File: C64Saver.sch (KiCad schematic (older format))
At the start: 15 parts, among them J1 Power I/O, Q1 PN2222A, Q2 PN2222A

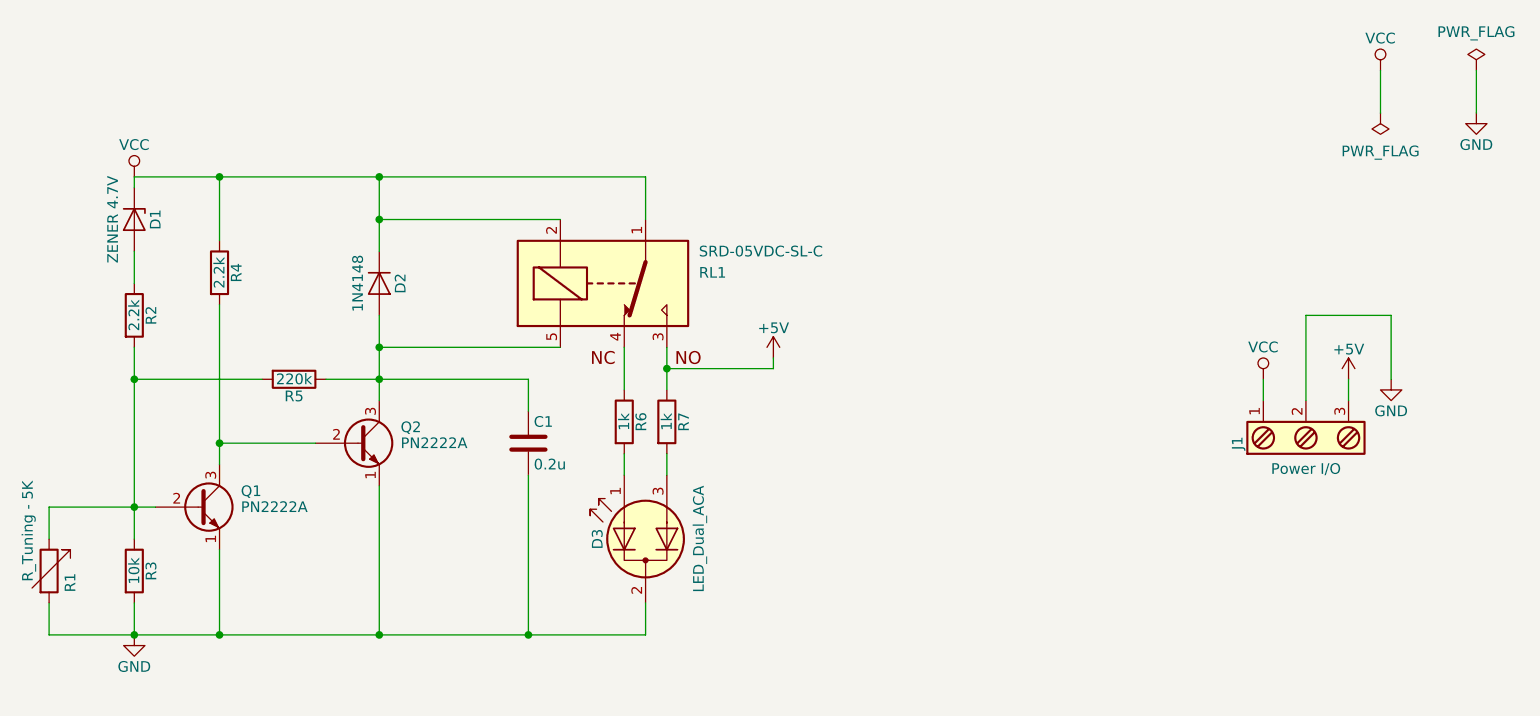
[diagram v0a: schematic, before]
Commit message: Relabel some components
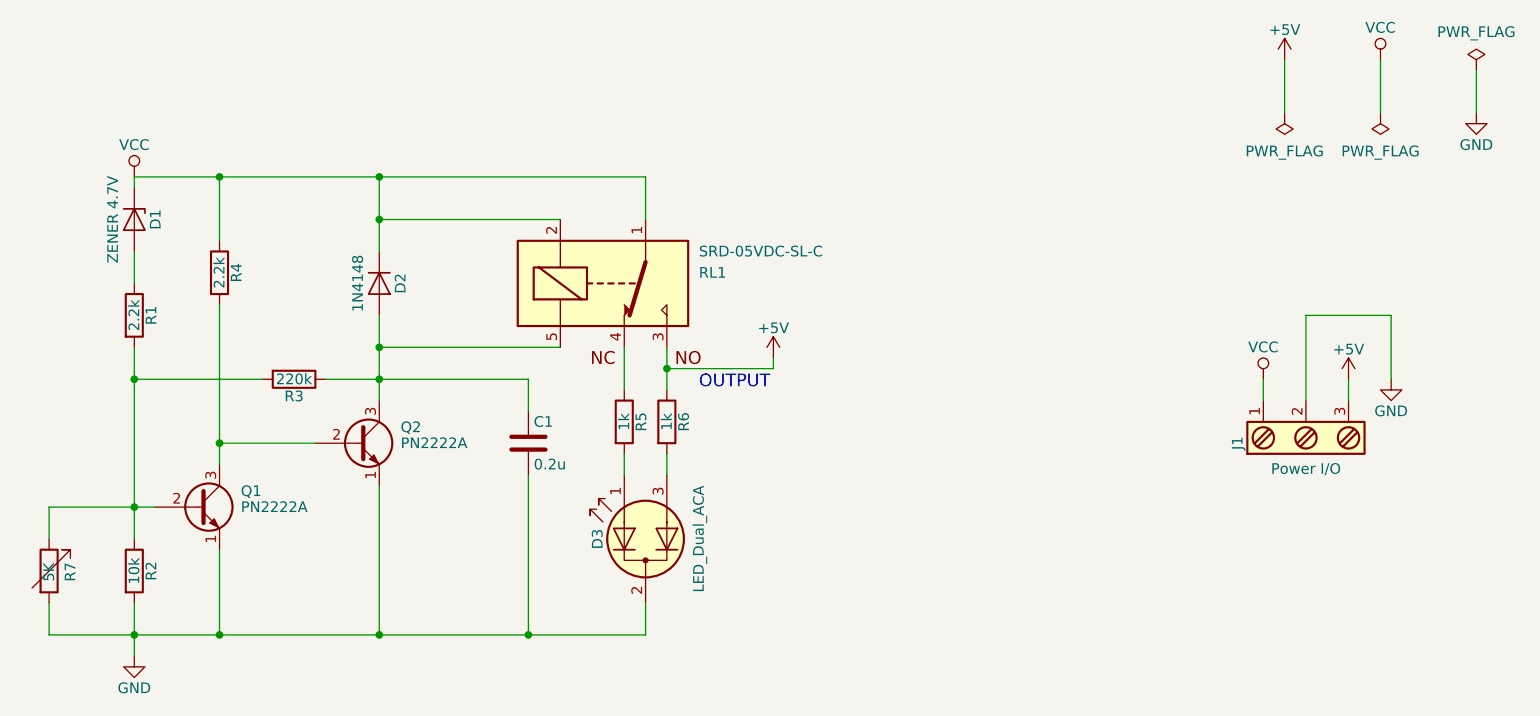
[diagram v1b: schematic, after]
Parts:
- R7: renamed from R1; value R_Tuning - 5K -> 5K
- renumbered R2 to R1, R3 to R2, R5 to R3, R6 to R5, R7 to R6
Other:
- note added: "OUTPUT"
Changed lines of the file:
@@
 $EndComp
 $Comp
-L R R3
+L R R2
 U 1 1 59765DBB
 P 4200 3200
-F 0 "R3" V 4280 3200 50  0000 C CNN
+F 0 "R2" V 4280 3200 50  0000 C CNN
 F 1 "10k" V 4200 3200 50  0000 C CNN
 F 2 "Resistors_SMD:R_0805_HandSoldering" V 4130 3200 50  0001 C CNN
@@
 L GND #PWR01
 U 1 1 59765E30
-P 4200 3500
-F 0 "#PWR01" H 4200 3250 50  0001 C CNN
-F 1 "GND" H 4200 3350 50  0000 C CNN
-F 2 "" H 4200 3500 50  0000 C CNN
-F 3 "" H 4200 3500 50  0000 C CNN
-	1    4200 3500
-	1    0    0    -1
-$EndComp
-$Comp
-L R R2
+P 4200 3600
+F 0 "#PWR01" H 4200 3350 50  0001 C CNN
+F 1 "GND" H 4200 3450 50  0000 C CNN
+F 2 "" H 4200 3600 50  0000 C CNN
+F 3 "" H 4200 3600 50  0000 C CNN
+	1    4200 3600
+	1    0    0    -1
+$EndComp
+$Comp
+L R R1
 U 1 1 59765E4A
 P 4200 2000
-F 0 "R2" V 4280 2000 50  0000 C CNN
+F 0 "R1" V 4280 2000 50  0000 C CNN
 F 1 "2.2k" V 4200 2000 50  0000 C CNN
 F 2 "Resistors_SMD:R_0805_HandSoldering" V 4130 2000 50  0001 C CNN
@@
 $EndComp
 $Comp
-L R R5
+L R R3
 U 1 1 5976603D
 P 4950 2300
-F 0 "R5" V 5030 2300 50  0000 C CNN
+F 0 "R3" V 5030 2300 50  0000 C CNN
 F 1 "220k" V 4950 2300 50  0000 C CNN
 F 2 "Resistors_SMD:R_0805_HandSoldering" V 4880 2300 50  0001 C CNN
@@
 	3800 2900 4300 2900
 Wire Wire Line
-	4200 3350 4200 3500
+	4200 3350 4200 3600
 Wire Wire Line
 	3800 3500 6600 3500
@@
 Connection ~ 5350 2150
 $Comp
-L R R6
+L R R5
 U 1 1 597671B5
 P 6500 2500
-F 0 "R6" V 6580 2500 50  0000 C CNN
+F 0 "R5" V 6580 2500 50  0000 C CNN
 F 1 "1k" V 6500 2500 50  0000 C CNN
 F 2 "Resistors_SMD:R_0805_HandSoldering" V 6430 2500 50  0001 C CNN
@@
 L VCC #PWR08
 U 1 1 59767AEF
-P 10050 850
-F 0 "#PWR08" H 10050 700 50  0001 C CNN
-F 1 "VCC" H 10050 1000 50  0000 C CNN
-F 2 "" H 10050 850 50  0000 C CNN
-F 3 "" H 10050 850 50  0000 C CNN
-	1    10050 850
+P 10050 800
+F 0 "#PWR08" H 10050 650 50  0001 C CNN
+F 1 "VCC" H 10050 950 50  0000 C CNN
+F 2 "" H 10050 800 50  0000 C CNN
+F 3 "" H 10050 800 50  0000 C CNN
+	1    10050 800
 	1    0    0    -1
 $EndComp
@@
 $EndComp
 Wire Wire Line
-	10050 850  10050 1050
+	10050 800  10050 1050
 Wire Wire Line
 	10500 850  10500 1050
@@
 	6600 3500 6600 3350
 $Comp
-L R R7
+L R R6
 U 1 1 59768A52
 P 6700 2500
-F 0 "R7" V 6780 2500 50  0000 C CNN
+F 0 "R6" V 6780 2500 50  0000 C CNN
 F 1 "1k" V 6700 2500 50  0000 C CNN
 F 2 "Resistors_SMD:R_0805_HandSoldering" V 6630 2500 50  0001 C CNN
@@
 Connection ~ 6700 2250
 $Comp
-L R_Variable R1
+L R_Variable R7
 U 1 1 59768CBA
 P 3800 3200
-F 0 "R1" V 3900 3100 50  0000 L CNN
-F 1 "R_Tuning - 5K" V 3700 3150 50  0000 L CNN
+F 0 "R7" V 3900 3150 50  0000 L CNN
+F 1 "5K" V 3800 3150 50  0000 L CNN
 F 2 "pth_resistors:trimmer_vishay_64w" V 3730 3200 50  0001 C CNN
 F 3 "" H 3800 3200 50  0000 C CNN
@@
 	0    -1   -1   0
 $EndComp
+$Comp
+L +5V #PWR011
+U 1 1 59AAFA20
+P 9600 800
+F 0 "#PWR011" H 9600 650 50  0001 C CNN
+F 1 "+5V" H 9600 940 50  0000 C CNN
+F 2 "" H 9600 800 50  0000 C CNN
+F 3 "" H 9600 800 50  0000 C CNN
+	1    9600 800
+	1    0    0    -1
+$EndComp
+$Comp
+L PWR_FLAG #FLG012
+U 1 1 59AAFA58
+P 9600 1050
+F 0 "#FLG012" H 9600 1145 50  0001 C CNN
+F 1 "PWR_FLAG" H 9600 1230 50  0000 C CNN
+F 2 "" H 9600 1050 50  0000 C CNN
+F 3 "" H 9600 1050 50  0000 C CNN
+	1    9600 1050
+	-1   0    0    1
+$EndComp
+Wire Wire Line
+	9600 1050 9600 800
+Text Notes 6850 2350 0    60   ~ 0
+OUTPUT
 $EndSCHEMATC
